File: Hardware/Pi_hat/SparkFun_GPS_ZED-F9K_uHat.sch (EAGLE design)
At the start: 38 parts, among them J4 U.FL, J7 RASPBERRYPI-40-PIN-GPIO_PTH_N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, U1 UBLOX_ZED_F9K, U3 TRIPLE_BUFFER_74LVC3G07

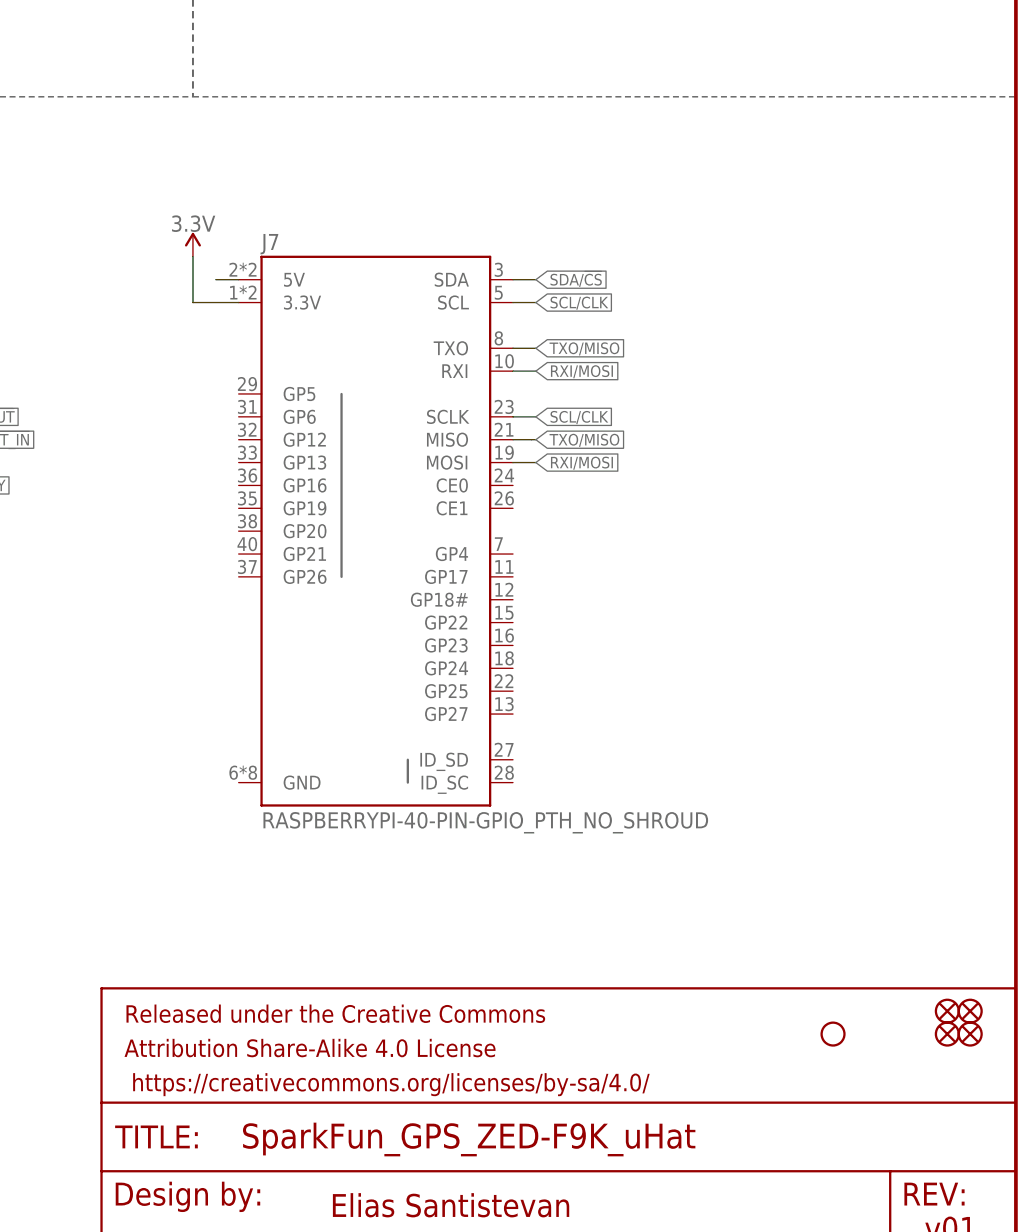
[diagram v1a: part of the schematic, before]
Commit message: Replaces micro hat with regular hat
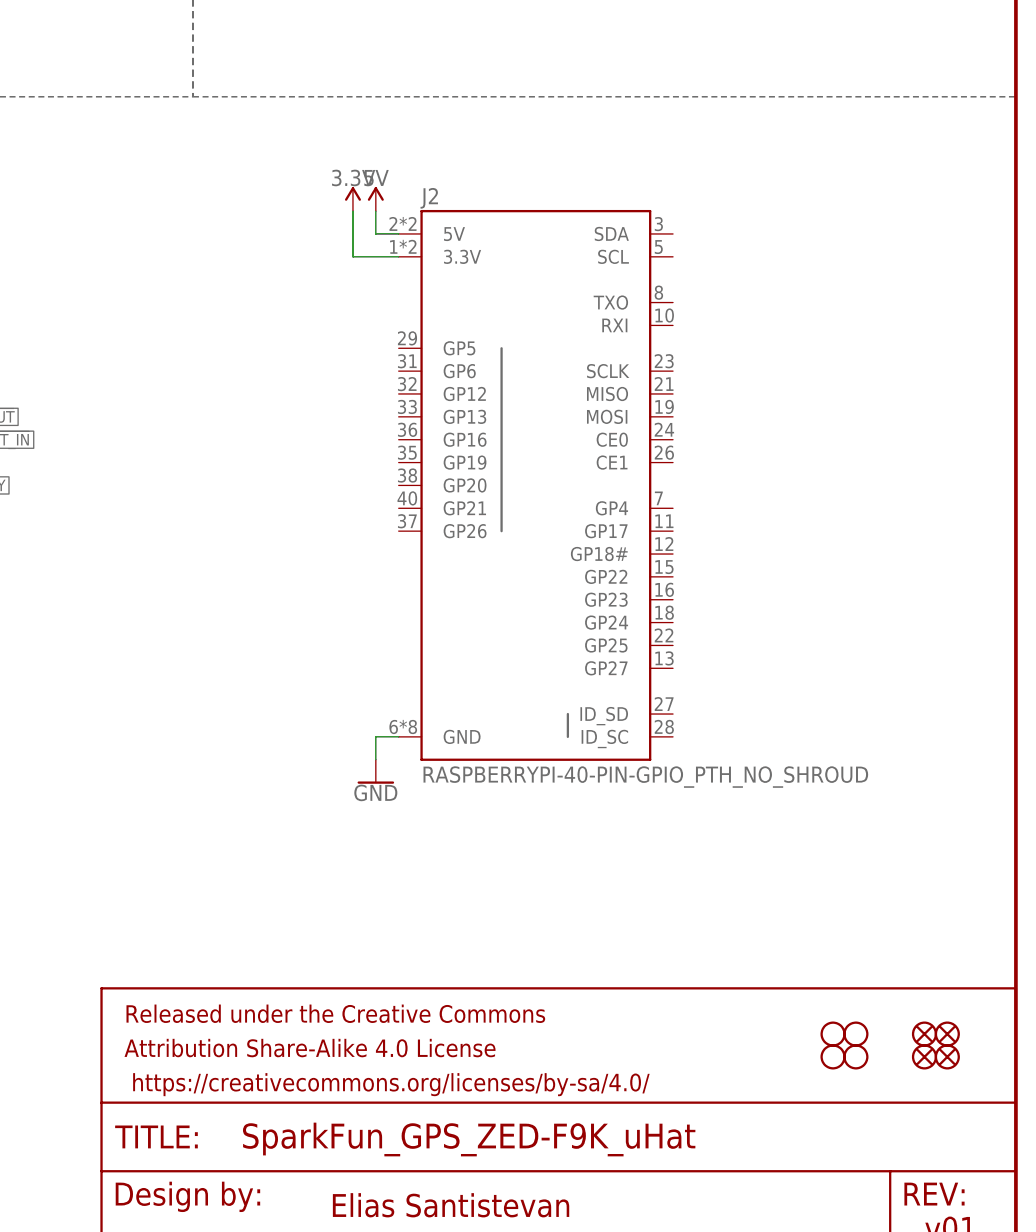
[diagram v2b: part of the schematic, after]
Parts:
- removed FD1, FD3, FD4: FIDUCIALUFIDUCIAL, SparkFun-Aesthetics:FIDUCIALUFIDUCIAL
- removed J7: RASPBERRYPI-40-PIN-GPIO_PTH_NO_SHROUD, SparkFun-Connectors:RASPBERRYPI-40-PIN-GPIO_PTH_NO_SHROUD
- added FD10, FD12, FD9: FIDUCIALUFIDUCIAL, SparkFun-Aesthetics:FIDUCIALUFIDUCIAL
- added H11, H12, H9: STAND-OFFTIGHT, SparkFun-Hardware:STAND-OFFTIGHT
- added J2: RASPBERRYPI-40-PIN-GPIO_PTH_NO_SHROUD, SparkFun-Connectors:RASPBERRYPI-40-PIN-GPIO_PTH_NO_SHROUD
- renumbered FD2 to FD11, H3 to H10
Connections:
- removed net N$10: J7.5V
- new net 5V: J2.5V
- net 3.3V: now also J2.3.3V; no longer J7.3.3V
- net GND: now also J2.GND
- net RXI/MOSI: no longer J7.MOSI, J7.RXI
- net SCL/CLK: no longer J7.SCL, J7.SCLK
- net SDA/!CS: no longer J7.SDA
- net TXO/MISO: no longer J7.MISO, J7.TXO
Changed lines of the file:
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@@
 <part name="SUPPLY1" library="SparkFun-PowerSymbols" deviceset="V_BATT" device=""/>
 <part name="SUPPLY3" library="SparkFun-PowerSymbols" deviceset="3.3V" device=""/>
-<part name="FD1" library="SparkFun-Aesthetics" deviceset="FIDUCIAL" device="UFIDUCIAL" value="FIDUCIALUFIDUCIAL"/>
-<part name="FD2" library="SparkFun-Aesthetics" deviceset="FIDUCIAL" device="UFIDUCIAL" value="FIDUCIALUFIDUCIAL"/>
-<part name="FD3" library="SparkFun-Aesthetics" deviceset="FIDUCIAL" device="UFIDUCIAL" value="FIDUCIALUFIDUCIAL"/>
-<part name="FD4" library="SparkFun-Aesthetics" deviceset="FIDUCIAL" device="UFIDUCIAL" value="FIDUCIALUFIDUCIAL"/>
-<part name="H3" library="SparkFun-Hardware" deviceset="STAND-OFF" device="TIGHT"/>
 <part name="JP1" library="SparkFun-Jumpers" deviceset="JUMPER-SMT_2_NO" device="_SILK"/>
 <part name="GND2" library="SparkFun-PowerSymbols" deviceset="GND" device=""/>
@@
 <part name="SUPPLY9" library="SparkFun-PowerSymbols" deviceset="3.3V" device=""/>
 <part name="GND11" library="SparkFun-PowerSymbols" deviceset="GND" device=""/>
-<part name="J7" library="SparkFun-Connectors" deviceset="RASPBERRYPI-40-PIN-GPIO" device="_PTH_NO_SHROUD"/>
-<part name="SUPPLY10" library="SparkFun-PowerSymbols" deviceset="3.3V" device=""/>
 <part name="GND16" library="SparkFun-PowerSymbols" deviceset="GND" device=""/>
 <part name="J8" library="SparkFun-Connectors" deviceset="USB_C" device="2-LAYER"/>
@@
 <part name="GND20" library="SparkFun-PowerSymbols" deviceset="GND" device=""/>
 <part name="SUPPLY12" library="SparkFun-PowerSymbols" deviceset="V_USB" device=""/>
+<part name="J2" library="SparkFun-Connectors" deviceset="RASPBERRYPI-40-PIN-GPIO" device="_PTH_NO_SHROUD"/>
+<part name="H9" library="SparkFun-Hardware" deviceset="STAND-OFF" device="TIGHT"/>
+<part name="H10" library="SparkFun-Hardware" deviceset="STAND-OFF" device="TIGHT"/>
+<part name="H11" library="SparkFun-Hardware" deviceset="STAND-OFF" device="TIGHT"/>
+<part name="H12" library="SparkFun-Hardware" deviceset="STAND-OFF" device="TIGHT"/>
+<part name="SUPPLY11" library="SparkFun-PowerSymbols" deviceset="3.3V" device=""/>
+<part name="SUPPLY15" library="SparkFun-PowerSymbols" deviceset="5V" device=""/>
+<part name="GND4" library="SparkFun-PowerSymbols" deviceset="GND" device=""/>
+<part name="FD9" library="SparkFun-Aesthetics" deviceset="FIDUCIAL" device="UFIDUCIAL"/>
+<part name="FD10" library="SparkFun-Aesthetics" deviceset="FIDUCIAL" device="UFIDUCIAL"/>
+<part name="FD11" library="SparkFun-Aesthetics" deviceset="FIDUCIAL" device="UFIDUCIAL"/>
+<part name="FD12" library="SparkFun-Aesthetics" deviceset="FIDUCIAL" device="UFIDUCIAL"/>
 </parts>
 <sheets>
@@
 <attribute name="VALUE" x="378.46" y="236.474" size="1.778" layer="96" align="bottom-center"/>
 </instance>
-<instance part="FD1" gate="G$1" x="426.72" y="33.02" smashed="yes"/>
-<instance part="FD2" gate="G$1" x="424.18" y="30.48" smashed="yes"/>
-<instance part="FD3" gate="G$1" x="426.72" y="30.48" smashed="yes"/>
-<instance part="FD4" gate="G$1" x="424.18" y="33.02" smashed="yes"/>
-<instance part="H3" gate="G$1" x="411.48" y="30.48" smashed="yes"/>
 <instance part="JP1" gate="G$1" x="203.2" y="66.04" smashed="yes">
 <attribute name="NAME" x="200.66" y="68.58" size="1.778" layer="95" font="vector"/>
@@
 <attribute name="VALUE" x="104.14" y="75.946" size="1.778" layer="96" align="top-center"/>
 </instance>
-<instance part="J7" gate="G$1" x="360.68" y="88.9" smashed="yes">
-<attribute name="NAME" x="347.98" y="117.602" size="1.778" layer="95"/>
-<attribute name="VALUE" x="347.98" y="53.34" size="1.778" layer="96"/>
-</instance>
-<instance part="SUPPLY10" gate="G$1" x="340.36" y="116.84" smashed="yes">
-<attribute name="VALUE" x="340.36" y="119.634" size="1.778" layer="96" align="bottom-center"/>
-</instance>
 <instance part="GND16" gate="1" x="228.6" y="190.5" smashed="yes">
 <attribute name="VALUE" x="226.06" y="187.96" size="1.778" layer="96" font="vector"/>
@@
 <attribute name="VALUE" x="231.14" y="228.854" size="1.778" layer="96" align="bottom-center"/>
 </instance>
+<instance part="J2" gate="G$1" x="378.46" y="93.98" smashed="yes">
+<attribute name="NAME" x="365.76" y="122.682" size="1.778" layer="95"/>
+<attribute name="VALUE" x="365.76" y="58.42" size="1.778" layer="96"/>
+</instance>
+<instance part="H9" gate="G$1" x="411.48" y="27.94" smashed="yes"/>
+<instance part="H10" gate="G$1" x="411.48" y="30.48" smashed="yes"/>
+<instance part="H11" gate="G$1" x="414.02" y="30.48" smashed="yes"/>
+<instance part="H12" gate="G$1" x="414.02" y="27.94" smashed="yes"/>
+<instance part="SUPPLY11" gate="G$1" x="358.14" y="121.92" smashed="yes">
+<attribute name="VALUE" x="358.14" y="124.714" size="1.778" layer="96" align="bottom-center"/>
+</instance>
+<instance part="SUPPLY15" gate="G$1" x="360.68" y="121.92" smashed="yes">
+<attribute name="VALUE" x="360.68" y="124.714" size="1.778" layer="96" align="bottom-center"/>
+</instance>
+<instance part="GND4" gate="1" x="360.68" y="58.42" smashed="yes">
+<attribute name="VALUE" x="360.68" y="58.166" size="1.778" layer="96" align="top-center"/>
+</instance>
+<instance part="FD9" gate="G$1" x="421.64" y="30.48" smashed="yes"/>
+<instance part="FD10" gate="G$1" x="421.64" y="27.94" smashed="yes"/>
+<instance part="FD11" gate="G$1" x="424.18" y="30.48" smashed="yes"/>
+<instance part="FD12" gate="G$1" x="424.18" y="27.94" smashed="yes"/>
 </instances>
 <busses>
@@
 <wire x1="236.22" y1="195.58" x2="236.22" y2="193.04" width="0.1524" layer="91"/>
 </segment>
+<segment>
+<pinref part="J2" gate="G$1" pin="GND"/>
+<wire x1="363.22" y1="63.5" x2="360.68" y2="63.5" width="0.1524" layer="91"/>
+<wire x1="360.68" y1="63.5" x2="360.68" y2="60.96" width="0.1524" layer="91"/>
+<pinref part="GND4" gate="1" pin="GND"/>
+</segment>
 </net>
 <net name="3.3V" class="0">
@@
 </segment>
 <segment>
-<pinref part="J7" gate="G$1" pin="3.3V"/>
-<wire x1="345.44" y1="111.76" x2="340.36" y2="111.76" width="0.1524" layer="91"/>
-<wire x1="340.36" y1="111.76" x2="340.36" y2="116.84" width="0.1524" layer="91"/>
-<pinref part="SUPPLY10" gate="G$1" pin="3.3V"/>
+<pinref part="J2" gate="G$1" pin="3.3V"/>
+<wire x1="363.22" y1="116.84" x2="358.14" y2="116.84" width="0.1524" layer="91"/>
+<wire x1="358.14" y1="116.84" x2="358.14" y2="121.92" width="0.1524" layer="91"/>
+<pinref part="SUPPLY11" gate="G$1" pin="3.3V"/>
 </segment>
 </net>
@@
 <wire x1="96.52" y1="231.14" x2="99.06" y2="231.14" width="0.1524" layer="91"/>
 <label x="99.06" y="231.14" size="1.27" layer="95" font="vector" xref="yes"/>
-</segment>
-<segment>
-<pinref part="J7" gate="G$1" pin="SCL"/>
-<wire x1="375.92" y1="111.76" x2="378.46" y2="111.76" width="0.1524" layer="91"/>
-<label x="378.46" y="111.76" size="1.27" layer="95" font="vector" xref="yes"/>
-</segment>
-<segment>
-<pinref part="J7" gate="G$1" pin="SCLK"/>
-<wire x1="375.92" y1="99.06" x2="378.46" y2="99.06" width="0.1524" layer="91"/>
-<label x="378.46" y="99.06" size="1.27" layer="95" font="vector" xref="yes"/>
 </segment>
 </net>
@@
 <label x="99.06" y="223.52" size="1.27" layer="95" font="vector" xref="yes"/>
 </segment>
-<segment>
-<pinref part="J7" gate="G$1" pin="TXO"/>
-<wire x1="375.92" y1="106.68" x2="378.46" y2="106.68" width="0.1524" layer="91"/>
-<label x="378.46" y="106.68" size="1.27" layer="95" font="vector" xref="yes"/>
-</segment>
-<segment>
-<pinref part="J7" gate="G$1" pin="MISO"/>
-<wire x1="375.92" y1="96.52" x2="377.952" y2="96.52" width="0.1524" layer="91"/>
-<wire x1="378.46" y1="96.52" x2="377.952" y2="96.52" width="0.1524" layer="91"/>
-<label x="378.46" y="96.52" size="1.27" layer="95" font="vector" xref="yes"/>
-</segment>
 </net>
 <net name="D_SEL" class="0">
@@
 <wire x1="96.52" y1="220.98" x2="99.06" y2="220.98" width="0.1524" layer="91"/>
 <label x="99.06" y="220.98" size="1.27" layer="95" font="vector" xref="yes"/>
-</segment>
-<segment>
-<pinref part="J7" gate="G$1" pin="RXI"/>
-<wire x1="375.92" y1="104.14" x2="378.46" y2="104.14" width="0.1524" layer="91"/>
-<label x="378.46" y="104.14" size="1.27" layer="95" font="vector" xref="yes"/>
-</segment>
-<segment>
-<pinref part="J7" gate="G$1" pin="MOSI"/>
-<wire x1="375.92" y1="93.98" x2="378.46" y2="93.98" width="0.1524" layer="91"/>
-<label x="378.46" y="93.98" size="1.27" layer="95" font="vector" xref="yes"/>
 </segment>
 </net>
@@
 <wire x1="213.36" y1="88.9" x2="213.36" y2="83.82" width="0.1524" layer="91"/>
 <wire x1="213.36" y1="83.82" x2="193.04" y2="83.82" width="0.1524" layer="91"/>
-</segment>
-<segment>
-<pinref part="J7" gate="G$1" pin="SDA"/>
-<wire x1="375.92" y1="114.3" x2="378.46" y2="114.3" width="0.1524" layer="91"/>
-<label x="378.46" y="114.3" size="1.27" layer="95" font="vector" xref="yes"/>
 </segment>
 </net>
@@
 </segment>
 </net>
-<net name="N$10" class="0">
-<segment>
-<pinref part="J7" gate="G$1" pin="5V"/>
-<wire x1="345.44" y1="114.3" x2="342.9" y2="114.3" width="0.1524" layer="91"/>
-</segment>
-</net>
 <net name="SHIELD" class="0">
 <segment>
@@
 </segment>
 </net>
+<net name="5V" class="0">
+<segment>
+<pinref part="J2" gate="G$1" pin="5V"/>
+<wire x1="363.22" y1="119.38" x2="360.68" y2="119.38" width="0.1524" layer="91"/>
+<wire x1="360.68" y1="119.38" x2="360.68" y2="121.92" width="0.1524" layer="91"/>
+<pinref part="SUPPLY15" gate="G$1" pin="5V"/>
+</segment>
+</net>
